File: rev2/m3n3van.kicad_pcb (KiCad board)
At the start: 2 copper layers, 242.4 x 75.7 mm, 118 parts, among them SW1 SW_Push, U1 SRV05-4, U2 ATmega32U4-AU, Y1 Resonator_Small

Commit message: Address review feedback
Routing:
- net GND: track 208.5 -> 86.2 mm, vias 35 -> 38
- net col7: track 87.9 -> 89.5 mm
- net Net-(H6-Pad1): track 30.8 -> 30.2 mm

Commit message: Update rev2 for production
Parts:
- C7: footprint Capacitor_SMD:C_0603_1608Metric -> Capacitor_SMD:C_0402_1005Metric
- moved C7 0.18 mm to (304.9, 230.2)

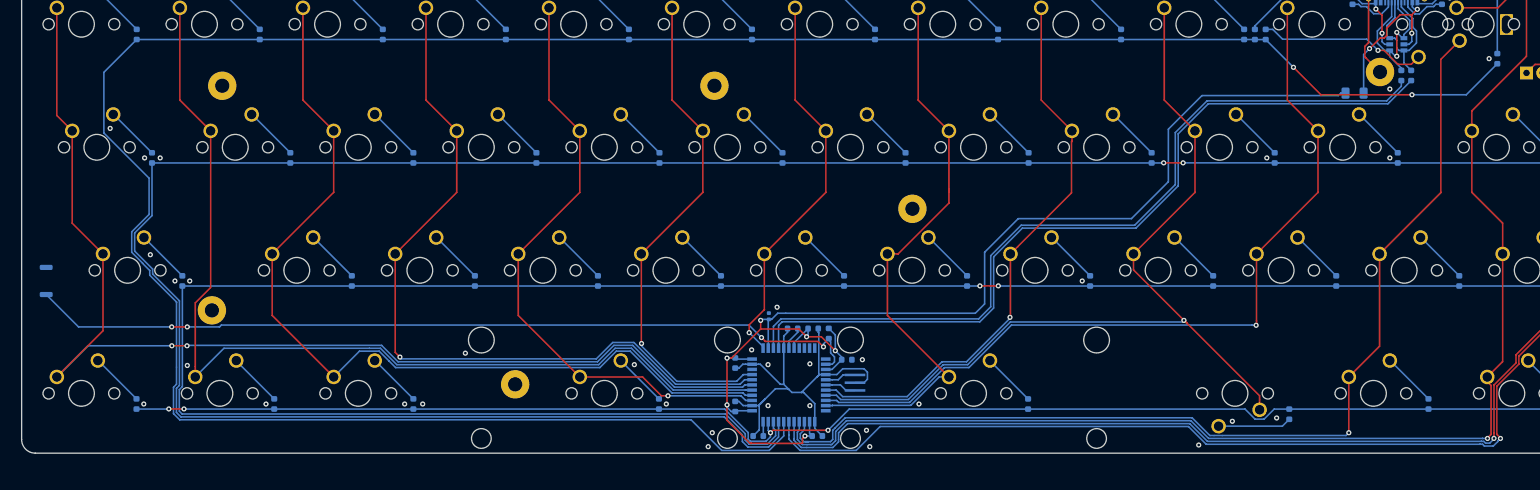
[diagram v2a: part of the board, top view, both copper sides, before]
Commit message: Add second encoder, RGB header, switch to assembly resonator footprint
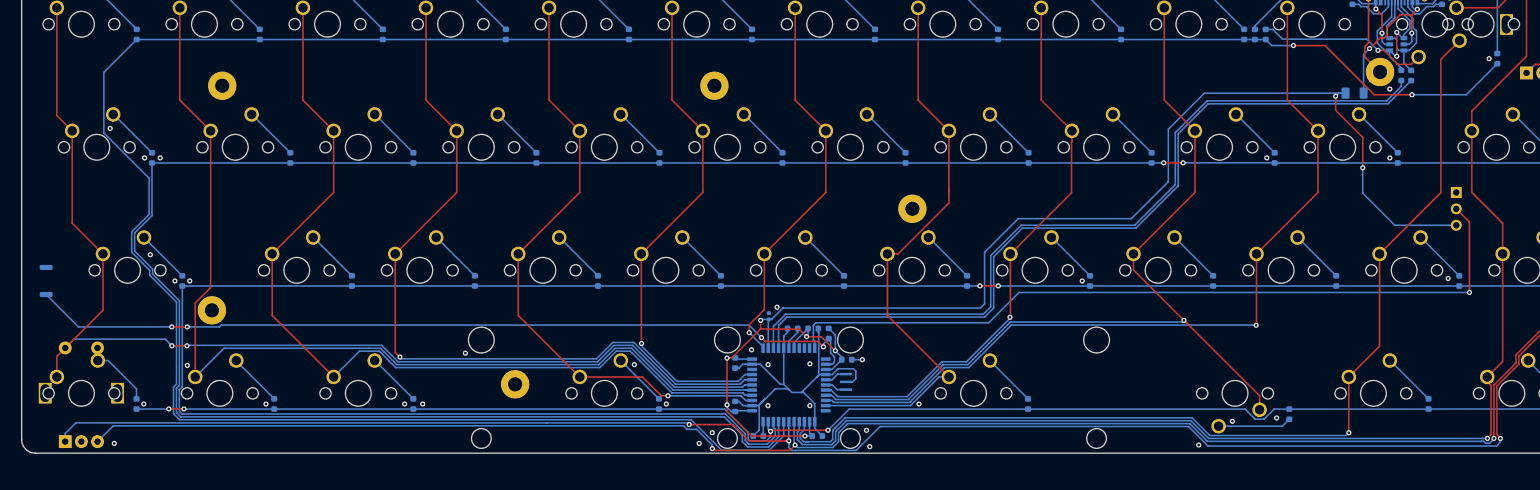
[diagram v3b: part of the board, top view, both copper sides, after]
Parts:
- added J1: Conn_01x03, Connector_PinHeader_2.54mm:PinHeader_1x03_P2.54mm_Vertical, B.Cu at (411.3, 211.0)
- added SW_2: Rotary_Encoder_Switch, Rotary_Encoder:RotaryEncoder_Alps_EC11E-Switch_Vertical_H20mm, F.Cu at (195.9, 249.6)
- Y1: footprint Crystal:Resonator_SMD_muRata_CSTxExxV-3Pin_3.0x1.1mm_HandSoldering -> Crystal:Resonator_SMD_muRata_CSTxExxV-3Pin_3.0x1.1mm
- moved Y1 1.40 mm to (316.8, 240.3)
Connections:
- U2 pad 11: Net-(U2-Pad11) -> B3
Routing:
- net B3: track 0.00 -> 121.1 mm, vias 0 -> 1
- net rotA: track 186.0 -> 302.2 mm, vias 1 -> 3
- net rotB: track 177.1 -> 288.7 mm, vias 1 -> 3
- net +5V: track 190.8 -> 223.5 mm, vias 6 -> 8
- net Net-(D_38-Pad2): track 8.44 -> 11.3 mm
- net col0: track 177.7 -> 175.4 mm
- net Net-(U2-Pad17): track 4.88 -> 3.43 mm
- net Net-(U2-Pad16): track 4.84 -> 3.49 mm
- net GND: track 86.2 -> 85.6 mm, vias 38 -> 40
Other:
- board text added: "GND B3 +5V"

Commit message: Update components, production files
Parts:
- C7: footprint Capacitor_SMD:C_0402_1005Metric -> Capacitor_SMD:C_0603_1608Metric
- D_1, D_10, D_11, D_12, D_13, D_14, D_15, D_16, D_17, D_18, D_19, D_2, D_20, D_21, D_22, D_23, D_24, D_25, D_26, D_27, D_28, D_29, D_3, D_30, D_31, D_32, D_33, D_34, D_35, D_36, D_37, D_38, D_39, D_4, D_40, D_41, D_42, D_43, D_44, D_45, D_5, D_6, D_7, D_8, D_9: footprint Diode_SMD:D_0603_1608Metric -> Diode_SMD:D_SOD-123
- moved D_12 33.7 mm to (415.2, 190.3)
- moved D_11 1.33 mm to (381.4, 186.5)
- moved D_43 1.17 mm to (384.6, 246.2)
- moved D_10 1.06 mm to (377.4, 186.5)
- moved D_1 1.02 mm to (206.0, 186.5)
- moved D_14 1.02 mm to (208.3, 205.6)
- moved D_18 1.02 mm to (286.9, 205.6)
- moved D_19 1.02 mm to (306.0, 205.6)
- moved D_20 1.02 mm to (325.0, 205.6)
- moved D_23 1.02 mm to (382.2, 205.6)
- moved D_24 1.02 mm to (401.2, 205.6)
- moved D_25 1.02 mm to (425.1, 205.6)
- moved D_28 1.02 mm to (258.3, 224.7)
- moved D_29 1.02 mm to (277.4, 224.7)
- moved D_32 1.02 mm to (334.5, 224.7)
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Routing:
- net Net-(D_12-Pad2): track 26.4 -> 10.4 mm, vias 1 -> 0
- net row0: track 383.3 -> 381.1 mm
- net row2: track 332.8 -> 334.6 mm
- net Net-(D_11-Pad2): track 14.1 -> 12.7 mm
- net Net-(D_10-Pad2): track 8.45 -> 7.15 mm
- net Net-(D_25-Pad2): track 8.55 -> 7.27 mm
- net Net-(D_7-Pad2): track 8.45 -> 7.17 mm
- net Net-(D_6-Pad2): track 8.45 -> 7.17 mm
- net Net-(D_5-Pad2): track 8.45 -> 7.17 mm
- net Net-(D_1-Pad2): track 8.45 -> 7.17 mm
- net Net-(D_2-Pad2): track 8.45 -> 7.17 mm
- net Net-(D_3-Pad2): track 8.45 -> 7.17 mm
- net Net-(D_8-Pad2): track 8.45 -> 7.17 mm
- net Net-(D_9-Pad2): track 8.45 -> 7.17 mm
- net Net-(D_4-Pad2): track 8.45 -> 7.17 mm
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
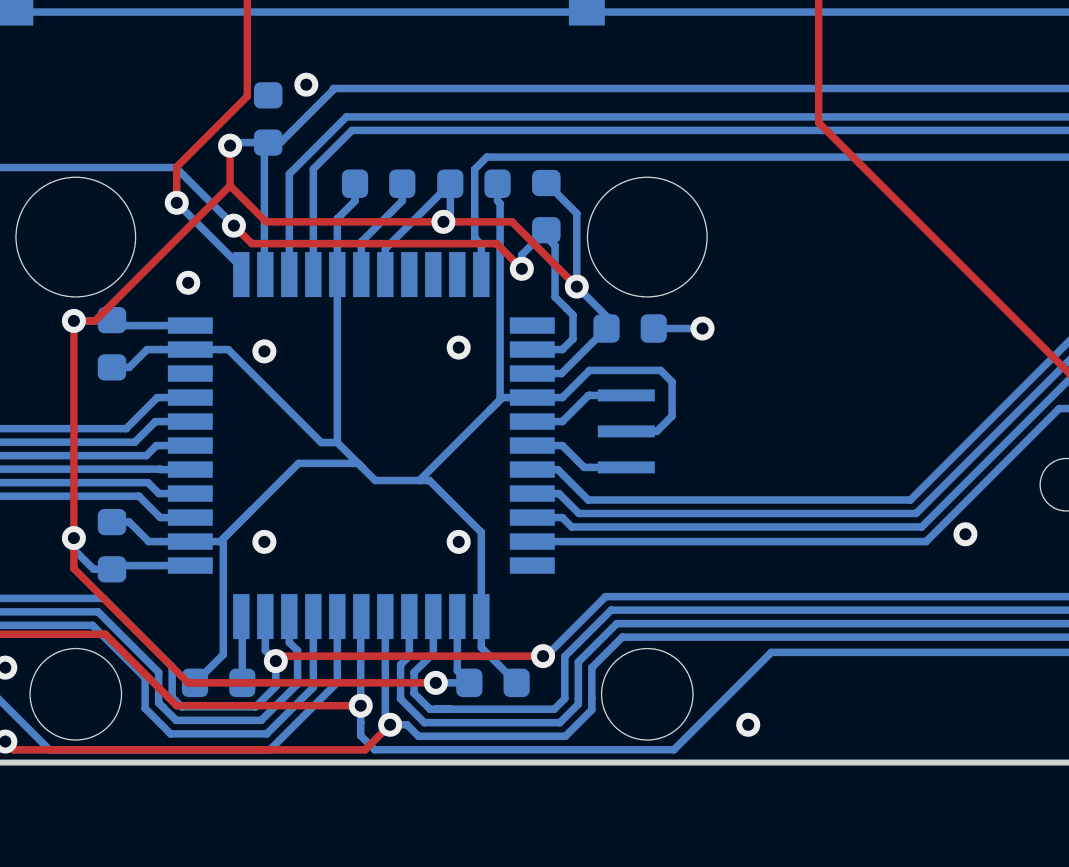
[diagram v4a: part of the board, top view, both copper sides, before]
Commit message: Switch to crystal, add MU dual footprint
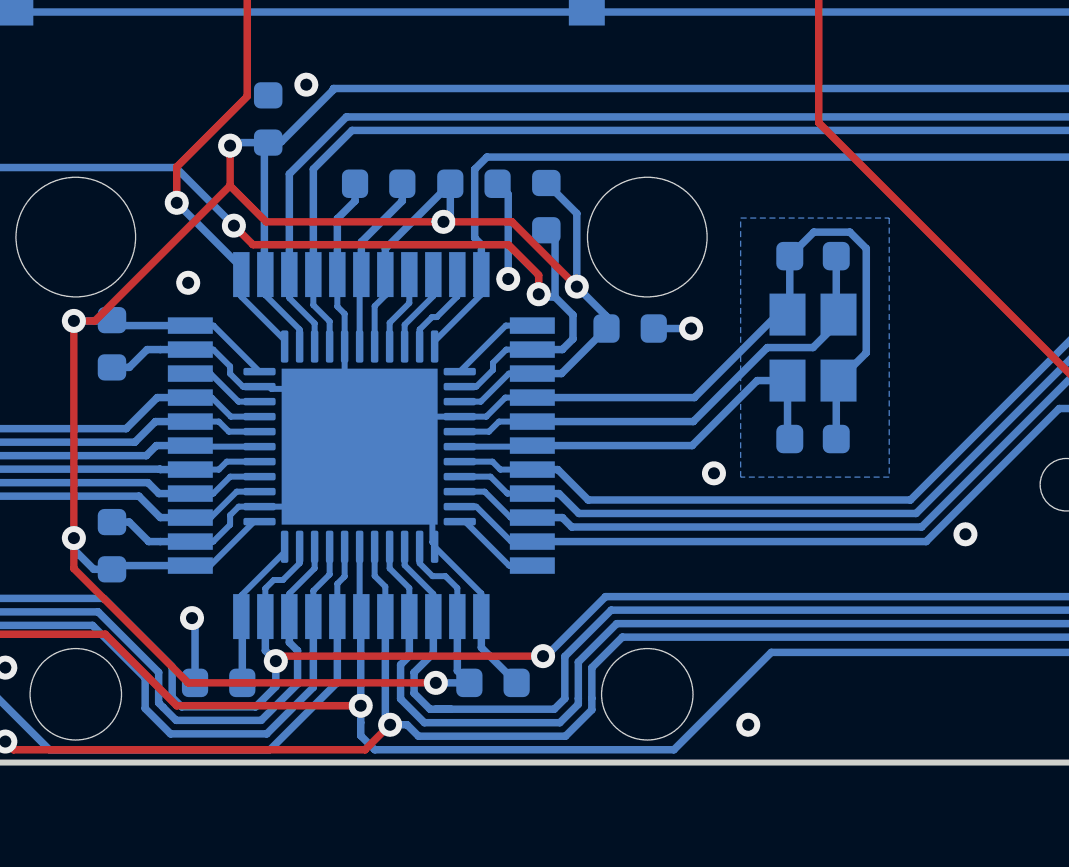
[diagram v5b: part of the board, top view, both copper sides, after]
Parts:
- added C8: 22pF, Capacitor_SMD:C_0603_1608Metric, B.Cu at (323.0, 240.6)
- added C9: 22pF, Capacitor_SMD:C_0603_1608Metric, B.Cu at (323.0, 234.5)
- added U3: ATmega32U4-MU, Package_DFN_QFN:QFN-44-1EP_7x7mm_P0.5mm_EP5.2x5.2mm, B.Cu at (307.9, 240.8)
- Y1: value Resonator_Small -> 16MHz; footprint Crystal:Resonator_SMD_muRata_CSTxExxV-3Pin_3.0x1.1mm -> Crystal:Crystal_SMD_3225-4Pin_3.2x2.5mm
- moved Y1 6.82 mm to (323.0, 237.5)
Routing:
- net +5V: track 223.4 -> 240.6 mm
- net Net-(C9-Pad2): track 3.49 -> 16.4 mm
- net Net-(C8-Pad1): track 3.43 -> 13.8 mm
- net GND: track 85.6 -> 91.7 mm, vias 29 -> 28
- net Net-(R1-Pad2): track 131.1 -> 134.4 mm
- net Net-(U2-Pad12): track 0.00 -> 3.06 mm
- net B3: track 121.6 -> 124.6 mm
- net Net-(U2-Pad22): track 0.00 -> 3.03 mm
- net Net-(U2-Pad10): track 0.00 -> 3.01 mm
- net col6: track 60.5 -> 63.5 mm
- net row3: track 228.6 -> 231.6 mm
- net Net-(R6-Pad2): track 2.22 -> 5.15 mm
- net col7: track 89.5 -> 92.4 mm
- net Net-(U2-Pad9): track 0.00 -> 2.79 mm
- net col10: track 126.8 -> 129.6 mm
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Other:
- rule trace_min: 0.2 -> 0.128
